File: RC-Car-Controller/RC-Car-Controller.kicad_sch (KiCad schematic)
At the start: 4 parts

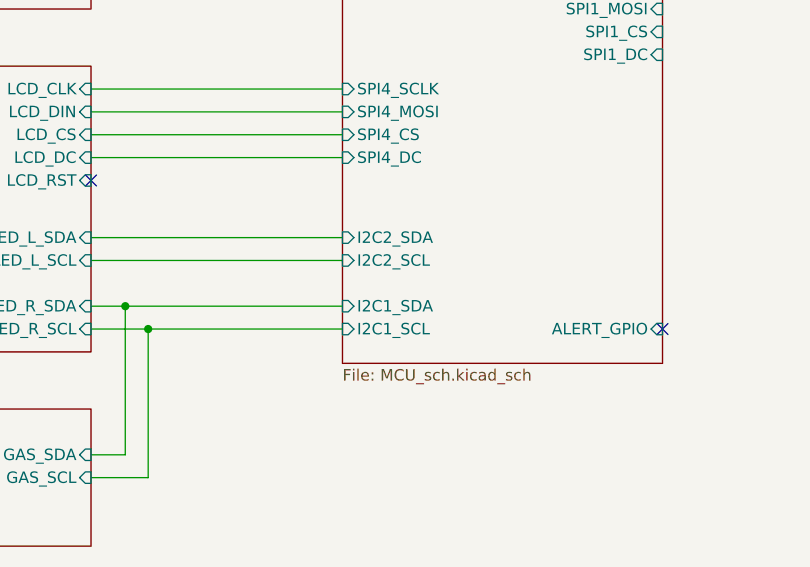
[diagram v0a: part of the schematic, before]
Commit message: Finished non-RF Controller PCB
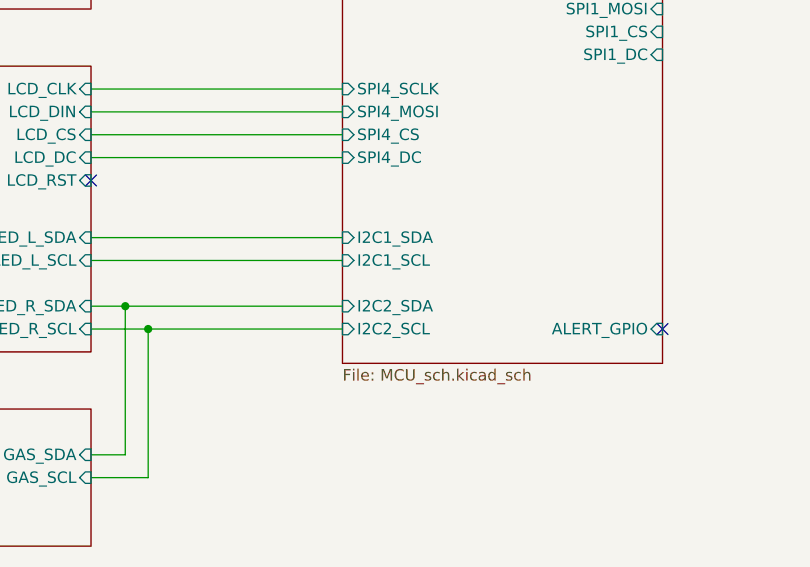
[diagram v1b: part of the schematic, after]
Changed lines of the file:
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@@
 	(paper "A4")
+	(junction
+		(at 91.44 151.13)
+		(diameter 0)
+		(color 0 0 0 0)
+	)
 	(junction
 		(at 74.93 40.64)
@@
 	)
 	(junction
-		(at 91.44 151.13)
-		(diameter 0)
-		(color 0 0 0 0)
-	)
-	(junction
 		(at 88.9 148.59)
 		(diameter 0)
@@
 	(wire
 		(pts
+			(xy 85.09 151.13) (xy 91.44 151.13)
+		)
+		(stroke
+			(width 0)
+			(type default)
+		)
+	)
+	(wire
+		(pts
+			(xy 85.09 129.54) (xy 113.03 129.54)
+		)
+		(stroke
+			(width 0)
+			(type default)
+		)
+	)
+	(wire
+		(pts
 			(xy 85.09 140.97) (xy 113.03 140.97)
-		)
-		(stroke
-			(width 0)
-			(type default)
-		)
-	)
-	(wire
-		(pts
-			(xy 85.09 143.51) (xy 113.03 143.51)
-		)
-		(stroke
-			(width 0)
-			(type default)
-		)
-	)
-	(wire
-		(pts
-			(xy 85.09 151.13) (xy 91.44 151.13)
-		)
-		(stroke
-			(width 0)
-			(type default)
-		)
-	)
-	(wire
-		(pts
-			(xy 85.09 129.54) (xy 113.03 129.54)
-		)
-		(stroke
-			(width 0)
-			(type default)
-		)
-	)
-	(wire
-		(pts
-			(xy 91.44 151.13) (xy 113.03 151.13)
 		)
 		(stroke
@@
 	(wire
 		(pts
+			(xy 91.44 151.13) (xy 113.03 151.13)
+		)
+		(stroke
+			(width 0)
+			(type default)
+		)
+	)
+	(wire
+		(pts
 			(xy 91.44 167.64) (xy 91.44 151.13)
 		)
@@
 		(pts
 			(xy 148.59 95.25) (xy 165.1 95.25)
+		)
+		(stroke
+			(width 0)
+			(type default)
+		)
+	)
+	(wire
+		(pts
+			(xy 85.09 143.51) (xy 113.03 143.51)
 		)
 		(stroke
@@
 		)
 		(pin "I2C1_SCL" input
+			(at 113.03 143.51 180)
+			(effects
+				(font
+					(size 1.27 1.27)
+				)
+				(justify left)
+			)
+		)
+		(pin "I2C1_SDA" input
+			(at 113.03 140.97 180)
+			(effects
+				(font
+					(size 1.27 1.27)
+				)
+				(justify left)
+			)
+		)
+		(pin "I2C2_SCL" input
 			(at 113.03 151.13 180)
 			(effects
@@
 			)
 		)
-		(pin "I2C1_SDA" input
+		(pin "I2C2_SDA" input
 			(at 113.03 148.59 180)
 			(effects
 				(font
-					(size 1.27 1.27)
-				)
-				(justify left)
-			)
-		)
-		(pin "I2C2_SCL" input
-			(at 113.03 143.51 180)
-			(effects
-				(font
-					(size 1.27 1.27)
-				)
-				(justify left)
-			)
-		)
-		(pin "I2C2_SDA" input
-			(at 113.03 140.97 180)
-			(effects
-				(font

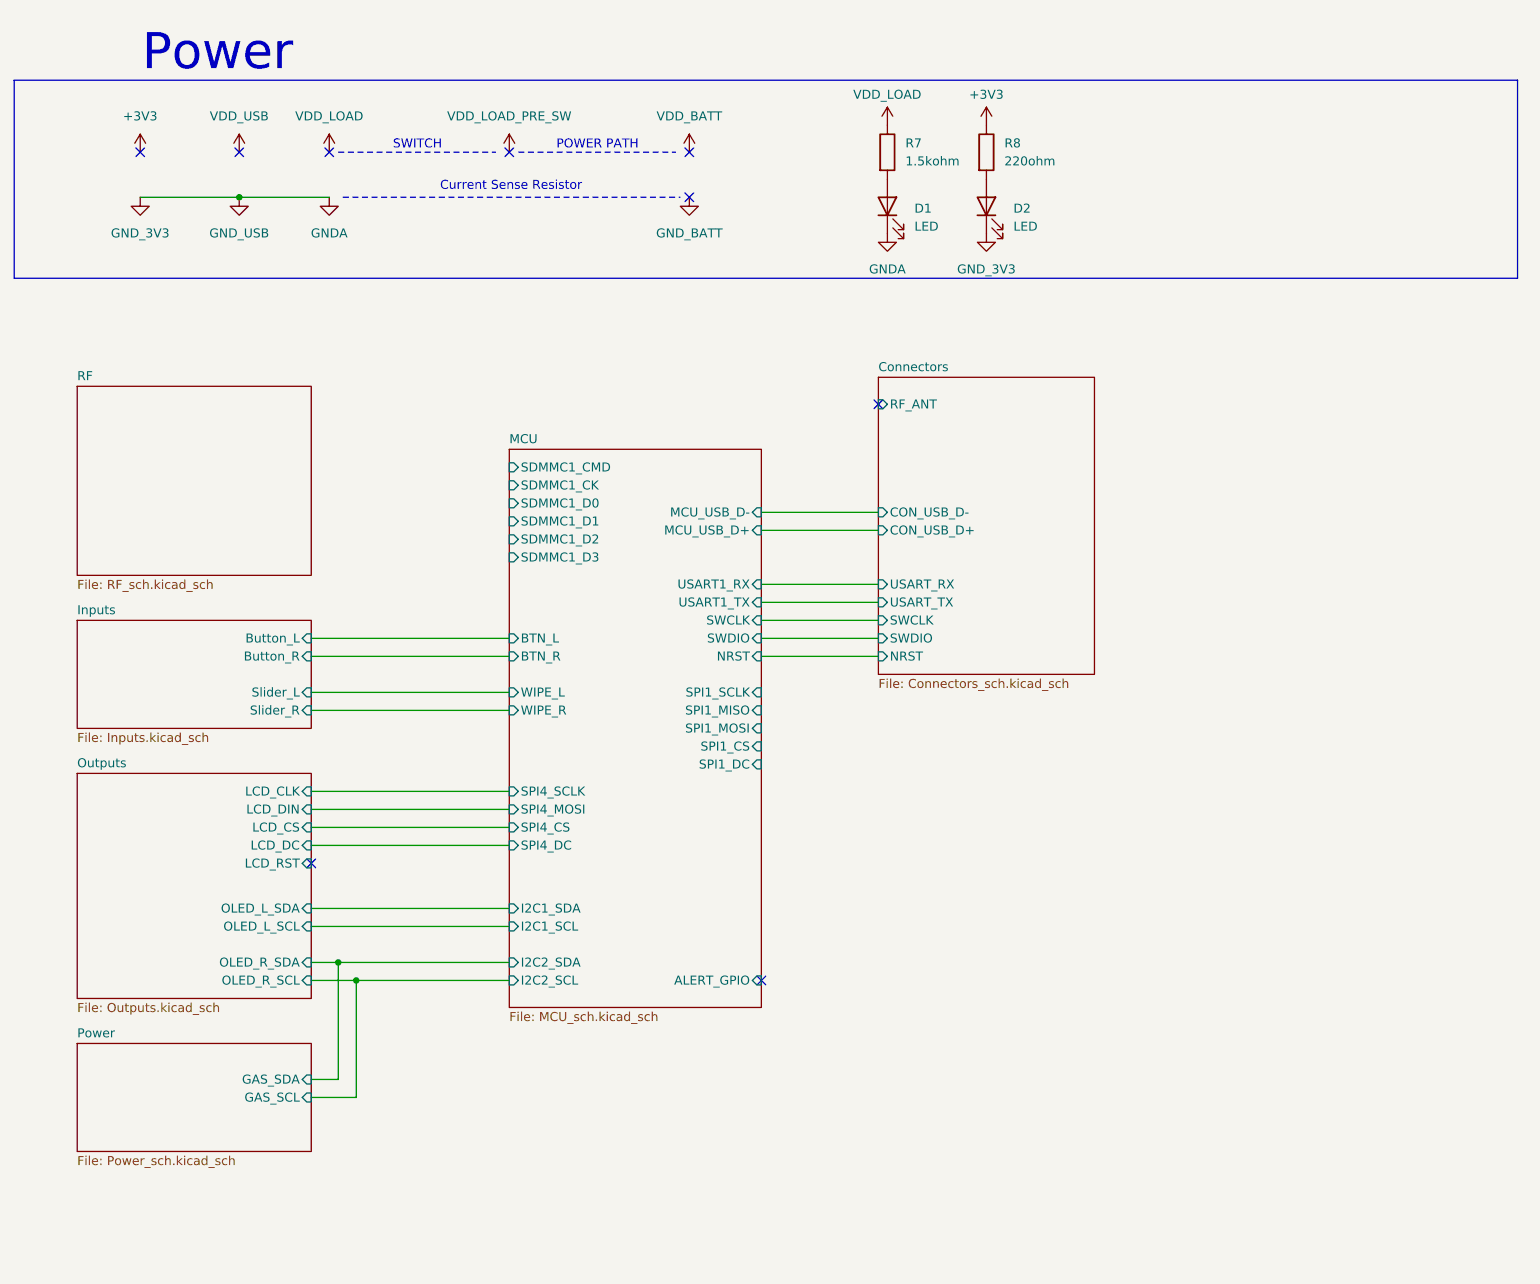
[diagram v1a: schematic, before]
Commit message: Added FGH100M footprint/schematic
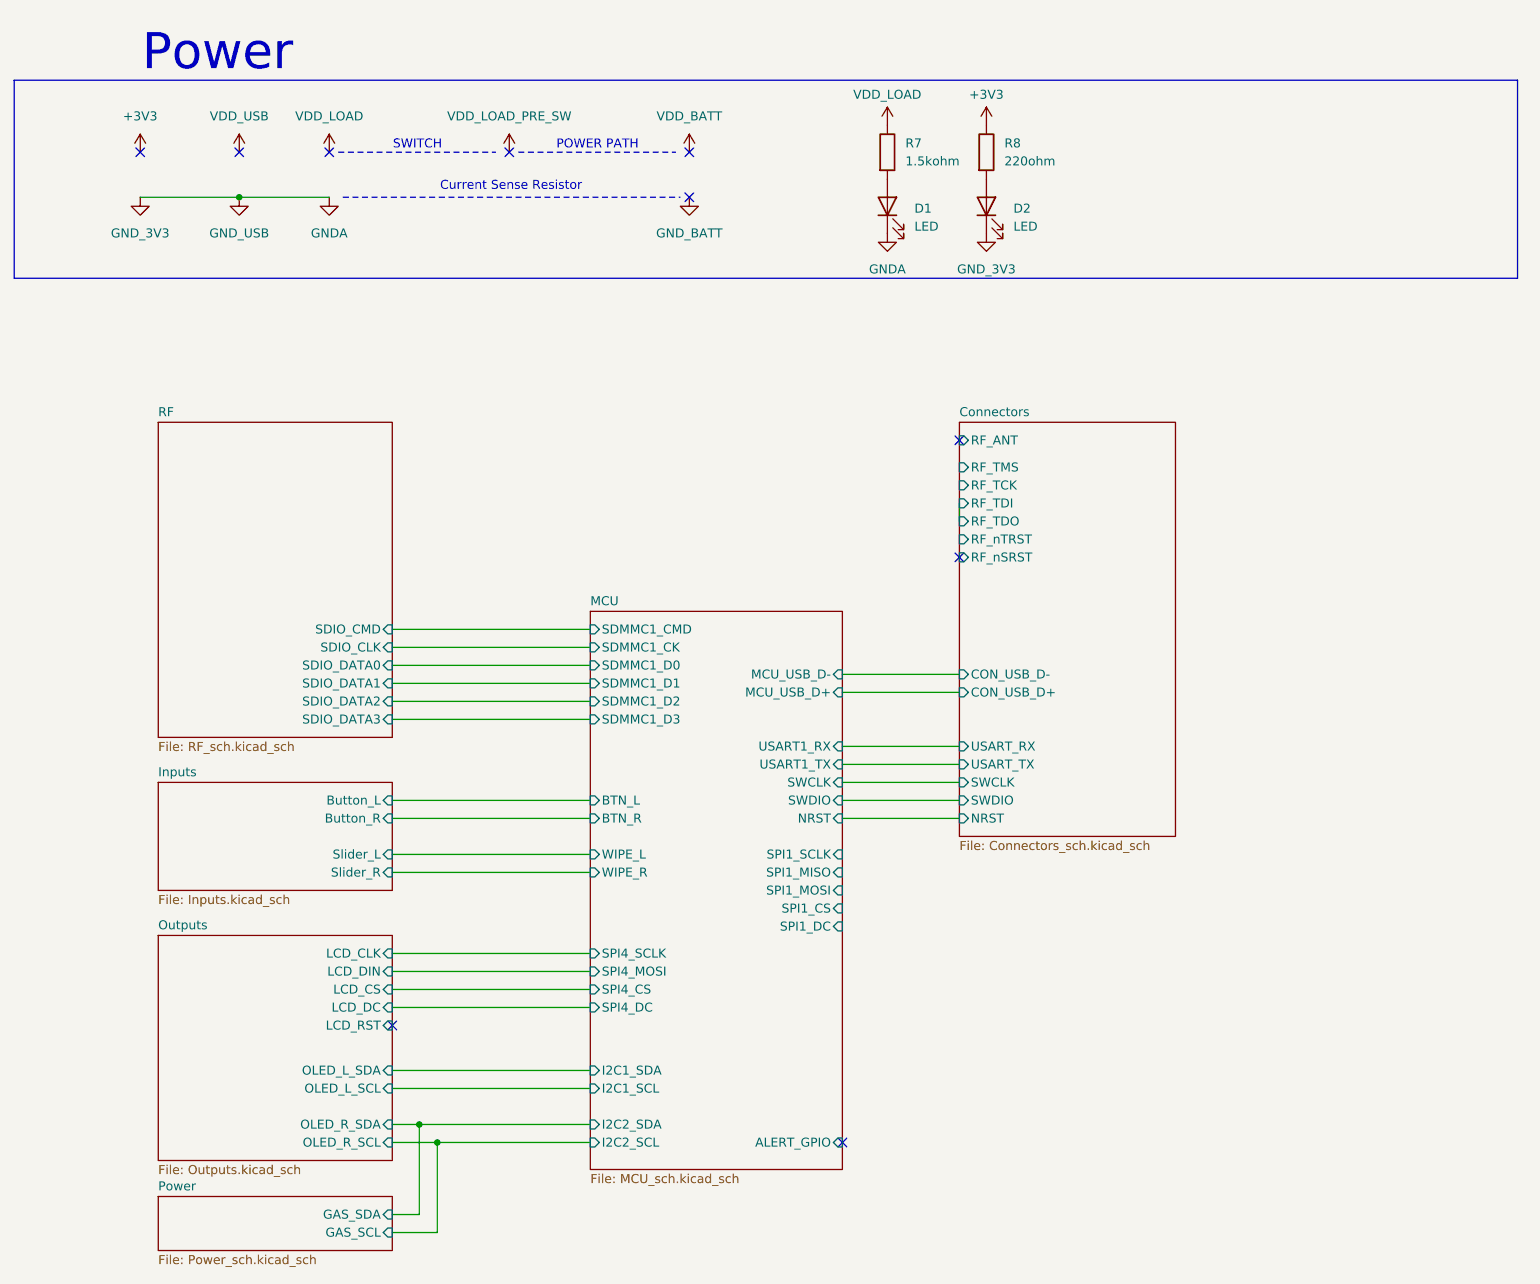
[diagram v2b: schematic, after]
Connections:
- no-connect marks 9 -> 10
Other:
- sheet Connectors ports: added RF_TCK, RF_TDI, RF_TDO, RF_TMS, RF_nSRST, RF_nTRST; removed none
- sheet RF ports: added SDIO_CLK, SDIO_CMD, SDIO_DATA0, SDIO_DATA1, SDIO_DATA2, SDIO_DATA3; removed none

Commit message: Wired up FGH100M
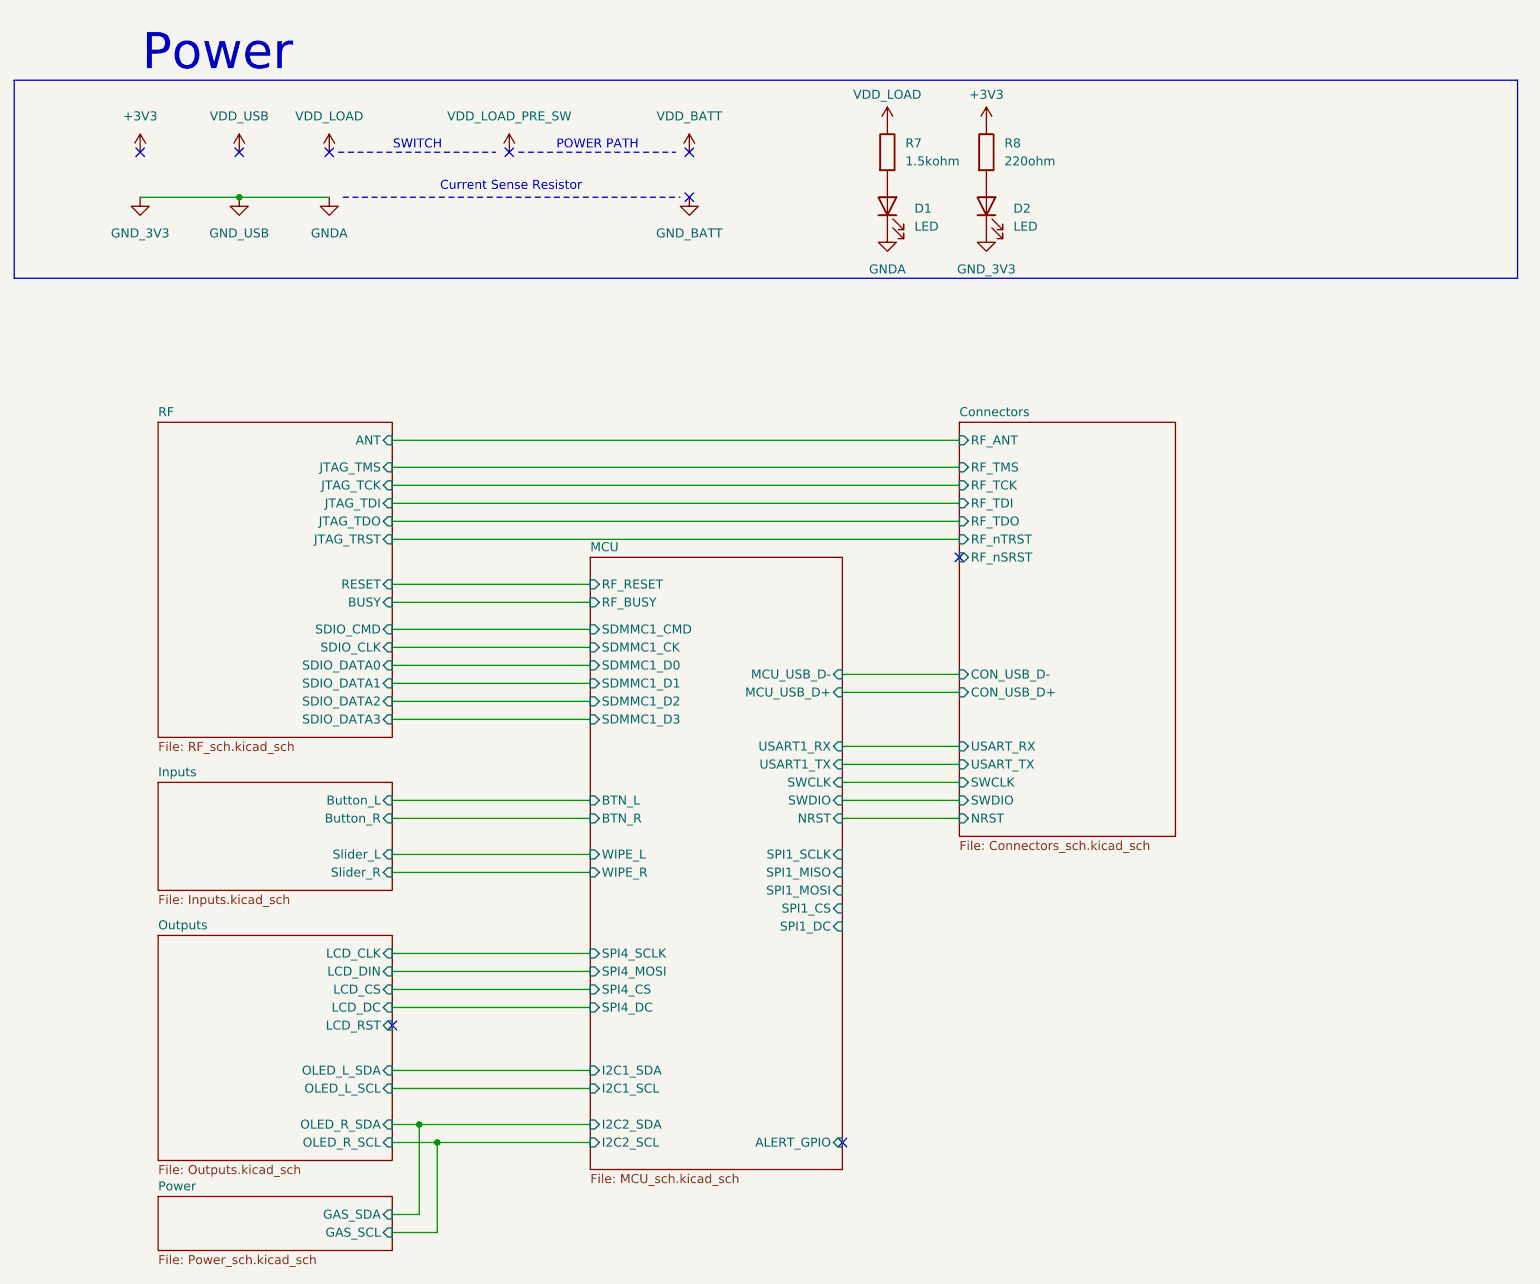
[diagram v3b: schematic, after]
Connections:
- no-connect marks 10 -> 9
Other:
- sheet MCU ports: added RF_BUSY, RF_RESET; removed none
- sheet RF ports: added ANT, BUSY, JTAG_TCK, JTAG_TDI, JTAG_TDO, JTAG_TMS, JTAG_TRST, RESET; removed none
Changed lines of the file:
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@@
-	)
-	(no_connect
-		(at 176.53 74.93)
 	)
 	(no_connect
@@
 	(wire
 		(pts
+			(xy 96.52 86.36) (xy 176.53 86.36)
+		)
+		(stroke
+			(width 0)
+			(type default)
+		)
+	)
+	(wire
+		(pts
 			(xy 96.52 163.83) (xy 124.46 163.83)
 		)
@@
 	(wire
 		(pts
+			(xy 96.52 95.25) (xy 124.46 95.25)
+		)
+		(stroke
+			(width 0)
+			(type default)
+		)
+	)
+	(wire
+		(pts
 			(xy 96.52 171.45) (xy 100.33 171.45)
 		)
@@
 	(wire
 		(pts
+			(xy 96.52 74.93) (xy 176.53 74.93)
+		)
+		(stroke
+			(width 0)
+			(type default)
+		)
+	)
+	(wire
+		(pts
+			(xy 96.52 78.74) (xy 176.53 78.74)
+		)
+		(stroke
+			(width 0)
+			(type default)
+		)
+	)
+	(wire
+		(pts
 			(xy 96.52 154.94) (xy 124.46 154.94)
 		)
@@
 	(wire
 		(pts
+			(xy 96.52 83.82) (xy 176.53 83.82)
+		)
+		(stroke
+			(width 0)
+			(type default)
+		)
+	)
+	(wire
+		(pts
 			(xy 160.02 125.73) (xy 176.53 125.73)
 		)
@@
 	(wire
 		(pts
-			(xy 176.53 86.36) (xy 176.53 83.82)
+			(xy 96.52 88.9) (xy 176.53 88.9)
+		)
+		(stroke
+			(width 0)
+			(type default)
+		)
+	)
+	(wire
+		(pts
+			(xy 96.52 81.28) (xy 176.53 81.28)
 		)
 		(stroke
@@
 		(pts
 			(xy 96.52 114.3) (xy 124.46 114.3)
+		)
+		(stroke
+			(width 0)
+			(type default)
+		)
+	)
+	(wire
+		(pts
+			(xy 96.52 97.79) (xy 124.46 97.79)
 		)
 		(stroke
@@
 			)
 		)
+		(pin "JTAG_TCK" input
+			(at 96.52 81.28 0)
+			(effects
+				(font
+					(size 1.27 1.27)
+				)
+				(justify right)
+			)
+		)
+		(pin "JTAG_TMS" input
+			(at 96.52 78.74 0)
+			(effects
+				(font
+					(size 1.27 1.27)
+				)
+				(justify right)
+			)
+		)
+		(pin "JTAG_TRST" input
+			(at 96.52 88.9 0)
+			(effects
+				(font
+					(size 1.27 1.27)
+				)
+				(justify right)
+			)
+		)
+		(pin "JTAG_TDI" input
+			(at 96.52 83.82 0)
+			(effects
+				(font
+					(size 1.27 1.27)
+				)
+				(justify right)
+			)
+		)
+		(pin "JTAG_TDO" input
+			(at 96.52 86.36 0)
+			(effects
+				(font
+					(size 1.27 1.27)
+				)
+				(justify right)
+			)
+		)
+		(pin "BUSY" input
+			(at 96.52 97.79 0)
+			(effects
+				(font
+					(size 1.27 1.27)
+				)
+				(justify right)
+			)
+		)
+		(pin "RESET" input
+			(at 96.52 95.25 0)
+			(effects
+				(font
+					(size 1.27 1.27)
+				)
+				(justify right)
+			)
+		)
+		(pin "ANT" input
+			(at 96.52 74.93 0)
+			(effects
+				(font
+					(size 1.27 1.27)
+				)
+				(justify right)
+			)
+		)
 		(instances
 			(project "RC-Car-Controller"
@@
 	)
 	(sheet
-		(at 124.46 99.06)
-		(size 35.56 78.74)
+		(at 124.46 91.44)
+		(size 35.56 86.36)
 		(fields_autoplaced yes)
 		(stroke
@@
 		)
 		(property "Sheetname" "MCU"
-			(at 124.46 98.3484 0)
+			(at 124.46 90.7284 0)
 			(effects
 				(font
@@
 			(effects
 				(font
+					(size 1.27 1.27)
+				)
+				(justify left)
+			)
+		)
+		(pin "RF_RESET" input
+			(at 124.46 95.25 180)
+			(effects
+				(font
+					(size 1.27 1.27)
+				)
+				(justify left)
+			)
+		)
+		(pin "RF_BUSY" input
+			(at 124.46 97.79 180)
+			(effects
+				(font

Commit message: Finished Controller PCB Pre-Review
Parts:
- added D3: LED, LED_THT:LED_D5.0mm, symbol Device:LED
- added R3: 60ohm, Resistor_SMD:R_0603_1608Metric, symbol Device:R
- added TP1, TP2, TP3, TP4, TP5, TP6: TestPoint, Connector_PinHeader_2.54mm:PinHeader_1x02_P2.54mm_Vertical, symbol Connector:TestPoint
- R1: renamed from R7; value 1.5kohm -> 220ohm
- renumbered R8 to R2
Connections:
- net +3V3: now also R3.1, TP5.1
- net GNDA: now also D3.1 (K), TP2.1, TP4.1, TP6.1
- net VDD_BATT: now also TP3.1
- net VDD_USB: now also TP1.1
- new net: D3.2 (A), R3.2
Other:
- sheet MCU ports: added none; removed SPI1_CS, SPI1_DC, SPI1_MISO, SPI1_MOSI, SPI1_SCLK

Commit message: Added functionality to the STM32 on the tank PCB
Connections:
- no-connect marks 9 -> 10
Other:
- sheet MCU ports: added none; removed RF_BUSY
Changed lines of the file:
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@@
 	)
 	(no_connect
+		(at 96.52 97.79)
+	)
+	(no_connect
 		(at 160.02 173.99)
 	)
@@
 	(wire
 		(pts
-			(xy 96.52 97.79) (xy 124.46 97.79)
-		)
-		(stroke
-			(width 0)
-			(type default)
-		)
-	)
-	(wire
-		(pts
 			(xy 96.52 147.32) (xy 124.46 147.32)
 		)
@@
 			(effects
 				(font
-					(size 1.27 1.27)
-				)
-				(justify left)
-			)
-		)
-		(pin "RF_BUSY" input
-			(at 124.46 97.79 180)
-			(effects
-				(font

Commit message: most resistors given PNs
most resistors given PNs. some remaining
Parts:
- R1, R2: MANUF_PN (none) -> RMCF0603FT220R
- R3: MANUF_PN (none) -> RMCF0603FT62R0
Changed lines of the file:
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@@
+			)
+		)
+		(property "MANUF_PN" ""
+			(at 238.149 31.1872 0)
+			(effects
+				(font
+					(size 1.27 1.27)
+				)
+				(hide yes)
 			)
 		)
@@
 			)
 		)
+		(property "MANUF_PN" ""
+			(at 180.34 41.91 0)
+			(effects
+				(font
+					(size 1.27 1.27)
+				)
+				(hide yes)
+			)
+		)
 		(pin "2"
 		)
@@
 			)
 		)
+		(property "MANUF_PN" ""
+			(at 238.149 45.1572 0)
+			(effects
+				(font
+					(size 1.27 1.27)
+				)
+				(hide yes)
+			)
+		)
 		(pin "1"
 		)
@@
 			)
 		)
+		(property "MANUF_PN" "RMCF0603FT62R0"
+			(at 195.58 34.29 0)
+			(effects
+				(font
+					(size 1.27 1.27)
+				)
+				(hide yes)
+			)
+		)
 		(pin "1"
 		)
@@
 			)
 		)
+		(property "MANUF_PN" "RMCF0603FT220R"
+			(at 166.37 34.29 0)
+			(effects
+				(font
+					(size 1.27 1.27)
+				)
+				(hide yes)
+			)
+		)
 		(pin "1"
 		)
@@
 			)
 		)
+		(property "MANUF_PN" ""
+			(at 227.989 45.1572 0)
+			(effects
+				(font
+					(size 1.27 1.27)
+				)
+				(hide yes)
+			)
+		)
 		(pin "1"
 		)
@@
 			)
 		)
+		(property "MANUF_PN" ""
+			(at 249.579 31.1872 0)
+			(effects
+				(font
+					(size 1.27 1.27)
+				)
+				(hide yes)
+			)
+		)
 		(pin "1"
 		)
@@
 			)
 		)
+		(property "MANUF_PN" ""
+			(at 166.37 41.91 0)
+			(effects
+				(font
+					(size 1.27 1.27)
+				)
+				(hide yes)
+			)
+		)
 		(pin "2"
 		)
@@
 			)
 		)
+		(property "MANUF_PN" ""
+			(at 227.989 31.1872 0)
+			(effects
+				(font
+					(size 1.27 1.27)
+				)
+				(hide yes)
+			)
+		)
 		(pin "1"
 		)
@@
 			)
 		)
+		(property "MANUF_PN" ""
+			(at 195.58 41.91 0)
+			(effects
+				(font
+					(size 1.27 1.27)
+				)
+				(hide yes)
+			)
+		)
 		(pin "2"
 		)
@@
 			)
 		)
+		(property "MANUF_PN" "RMCF0603FT220R"
+			(at 180.34 34.29 0)
+			(effects
+				(font
+					(size 1.27 1.27)
+				)
+				(hide yes)
+			)
+		)
 		(pin "1"
 		)
@@
 			(at 249.579 45.1572 0)
 			(effects
+				(font
+					(size 1.27 1.27)
+				)
+				(hide yes)
+			)
+		)
+		(property "MANUF_PN" ""
+			(at 249.579 45.1572 0)
+			(effects
